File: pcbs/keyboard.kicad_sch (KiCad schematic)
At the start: 214 parts, among them J1 MJ-4PP-9, J2 MJ-4PP-9, SW1 SW_PUSH, SW2 SW_PUSH, SW3 RotaryEncoder_Switch, U1 ProMicro, U3 ProMicro

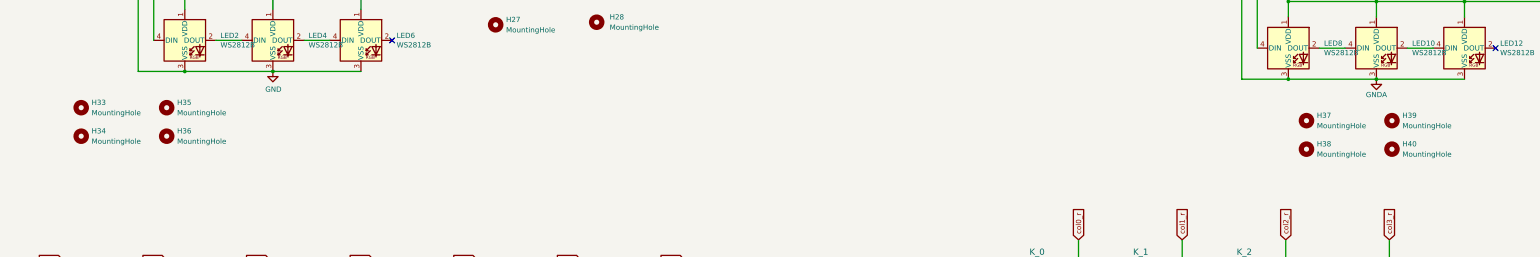
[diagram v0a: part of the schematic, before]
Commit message: Branch for a split jlcpcb order.
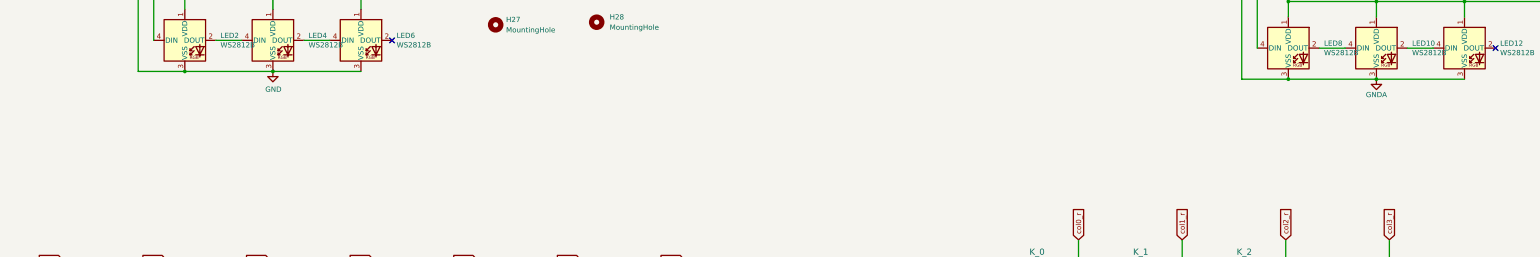
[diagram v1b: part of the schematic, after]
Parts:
- removed H33, H34, H35, H36, H37, H38, H39, H40: MountingHole, Keebio-Parts:breakaway-mousebites_fat-o-tesa, symbol Mechanical:MountingHole
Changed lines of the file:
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@@
     )
   )
-  (symbol (lib_id "Mechanical:MountingHole") (at 380.365 146.05 0) (unit 1)
-    (in_bom yes) (on_board yes) (dnp no) (fields_autoplaced)
-    (property "Reference" "H37" (at 382.905 144.78 0)
-      (effects (font (size 1.27 1.27)) (justify left))
-    )
-    (property "Value" "MountingHole" (at 382.905 147.32 0)
-      (effects (font (size 1.27 1.27)) (justify left))
-    )
-    (property "Footprint" "Keebio-Parts:breakaway-mousebites_fat-o-tesa" (at 380.365 146.05 0)
-      (effects (font (size 1.27 1.27)) hide)
-    )
-    (property "Datasheet" "~" (at 380.365 146.05 0)
-      (effects (font (size 1.27 1.27)) hide)
-    )
-    (instances
-      (project "keyboard"
-        (path "/30eea16d-cbc8-4652-9fea-1af3eb5fea52"
-          (reference "H37") (unit 1)
-        )
-      )
-    )
-  )
   (symbol (lib_id "Mechanical:MountingHole") (at 412.115 60.325 0) (unit 1)
     (in_bom yes) (on_board yes) (dnp no) (fields_autoplaced)
@@
     )
   )
-  (symbol (lib_id "Mechanical:MountingHole") (at 100.965 142.875 0) (unit 1)
-    (in_bom yes) (on_board yes) (dnp no) (fields_autoplaced)
-    (property "Reference" "H35" (at 103.505 141.605 0)
-      (effects (font (size 1.27 1.27)) (justify left))
-    )
-    (property "Value" "MountingHole" (at 103.505 144.145 0)
-      (effects (font (size 1.27 1.27)) (justify left))
-    )
-    (property "Footprint" "Keebio-Parts:breakaway-mousebites_fat-o-tesa" (at 100.965 142.875 0)
-      (effects (font (size 1.27 1.27)) hide)
-    )
-    (property "Datasheet" "~" (at 100.965 142.875 0)
-      (effects (font (size 1.27 1.27)) hide)
-    )
-    (instances
-      (project "keyboard"
-        (path "/30eea16d-cbc8-4652-9fea-1af3eb5fea52"
-          (reference "H35") (unit 1)
-        )
-      )
-    )
-  )
   (symbol (lib_id "Device:D_Small") (at 89.535 323.85 90) (unit 1)
     (in_bom yes) (on_board yes) (dnp no)
@@
     )
   )
-  (symbol (lib_id "Mechanical:MountingHole") (at 401.32 153.035 0) (unit 1)
-    (in_bom yes) (on_board yes) (dnp no) (fields_autoplaced)
-    (property "Reference" "H40" (at 403.86 151.765 0)
-      (effects (font (size 1.27 1.27)) (justify left))
-    )
-    (property "Value" "MountingHole" (at 403.86 154.305 0)
-      (effects (font (size 1.27 1.27)) (justify left))
-    )
-    (property "Footprint" "Keebio-Parts:breakaway-mousebites_fat-o-tesa" (at 401.32 153.035 0)
-      (effects (font (size 1.27 1.27)) hide)
-    )
-    (property "Datasheet" "~" (at 401.32 153.035 0)
-      (effects (font (size 1.27 1.27)) hide)
-    )
-    (instances
-      (project "keyboard"
-        (path "/30eea16d-cbc8-4652-9fea-1af3eb5fea52"
-          (reference "H40") (unit 1)
-        )
-      )
-    )
-  )
   (symbol (lib_id "MX_Alps_Hybrid:MX-NoLED") (at 167.005 265.43 0) (unit 1)
     (in_bom yes) (on_board yes) (dnp no)
@@
     )
   )
-  (symbol (lib_id "Mechanical:MountingHole") (at 380.365 153.035 0) (unit 1)
-    (in_bom yes) (on_board yes) (dnp no) (fields_autoplaced)
-    (property "Reference" "H38" (at 382.905 151.765 0)
-      (effects (font (size 1.27 1.27)) (justify left))
-    )
-    (property "Value" "MountingHole" (at 382.905 154.305 0)
-      (effects (font (size 1.27 1.27)) (justify left))
-    )
-    (property "Footprint" "Keebio-Parts:breakaway-mousebites_fat-o-tesa" (at 380.365 153.035 0)
-      (effects (font (size 1.27 1.27)) hide)
-    )
-    (property "Datasheet" "~" (at 380.365 153.035 0)
-      (effects (font (size 1.27 1.27)) hide)
-    )
-    (instances
-      (project "keyboard"
-        (path "/30eea16d-cbc8-4652-9fea-1af3eb5fea52"
-          (reference "H38") (unit 1)
-        )
-      )
-    )
-  )
   (symbol (lib_id "Device:D_Small") (at 516.255 320.04 90) (unit 1)
     (in_bom yes) (on_board yes) (dnp no)
@@
     )
   )
-  (symbol (lib_id "Mechanical:MountingHole") (at 80.01 142.875 0) (unit 1)
-    (in_bom yes) (on_board yes) (dnp no) (fields_autoplaced)
-    (property "Reference" "H33" (at 82.55 141.605 0)
-      (effects (font (size 1.27 1.27)) (justify left))
-    )
-    (property "Value" "MountingHole" (at 82.55 144.145 0)
-      (effects (font (size 1.27 1.27)) (justify left))
-    )
-    (property "Footprint" "Keebio-Parts:breakaway-mousebites_fat-o-tesa" (at 80.01 142.875 0)
-      (effects (font (size 1.27 1.27)) hide)
-    )
-    (property "Datasheet" "~" (at 80.01 142.875 0)
-      (effects (font (size 1.27 1.27)) hide)
-    )
-    (instances
-      (project "keyboard"
-        (path "/30eea16d-cbc8-4652-9fea-1af3eb5fea52"
-          (reference "H33") (unit 1)
-        )
-      )
-    )
-  )
   (symbol (lib_id "power:GND") (at 107.315 349.25 0) (unit 1)
     (in_bom yes) (on_board yes) (dnp no)
@@
     )
   )
-  (symbol (lib_id "Mechanical:MountingHole") (at 100.965 149.86 0) (unit 1)
-    (in_bom yes) (on_board yes) (dnp no) (fields_autoplaced)
-    (property "Reference" "H36" (at 103.505 148.59 0)
-      (effects (font (size 1.27 1.27)) (justify left))
-    )
-    (property "Value" "MountingHole" (at 103.505 151.13 0)
-      (effects (font (size 1.27 1.27)) (justify left))
-    )
-    (property "Footprint" "Keebio-Parts:breakaway-mousebites_fat-o-tesa" (at 100.965 149.86 0)
-      (effects (font (size 1.27 1.27)) hide)
-    )
-    (property "Datasheet" "~" (at 100.965 149.86 0)
-      (effects (font (size 1.27 1.27)) hide)
-    )
-    (instances
-      (project "keyboard"
-        (path "/30eea16d-cbc8-4652-9fea-1af3eb5fea52"
-          (reference "H36") (unit 1)
-        )
-      )
-    )
-  )
   (symbol (lib_id "PCM_marbastlib-mx:MX_stab") (at 361.315 341.63 0) (unit 1)
     (in_bom yes) (on_board yes) (dnp no) (fields_autoplaced)
@@
     )
   )
-  (symbol (lib_id "Mechanical:MountingHole") (at 80.01 149.86 0) (unit 1)
-    (in_bom yes) (on_board yes) (dnp no) (fields_autoplaced)
-    (property "Reference" "H34" (at 82.55 148.59 0)
-      (effects (font (size 1.27 1.27)) (justify left))
-    )
-    (property "Value" "MountingHole" (at 82.55 151.13 0)
-      (effects (font (size 1.27 1.27)) (justify left))
-    )
-    (property "Footprint" "Keebio-Parts:breakaway-mousebites_fat-o-tesa" (at 80.01 149.86 0)
-      (effects (font (size 1.27 1.27)) hide)
-    )
-    (property "Datasheet" "~" (at 80.01 149.86 0)
-      (effects (font (size 1.27 1.27)) hide)
-    )
-    (instances
-      (project "keyboard"
-        (path "/30eea16d-cbc8-4652-9fea-1af3eb5fea52"
-          (reference "H34") (unit 1)
-        )
-      )
-    )
-  )
   (symbol (lib_id "Mechanical:MountingHole") (at 159.385 81.915 0) (unit 1)
     (in_bom yes) (on_board yes) (dnp no)
@@
         )
       )
-    )
-  )
-  (symbol (lib_id "Mechanical:MountingHole") (at 401.32 146.05 0) (unit 1)
-    (in_bom yes) (on_board yes) (dnp no) (fields_autoplaced)
-    (property "Reference" "H39" (at 403.86 144.78 0)
-      (effects (font (size 1.27 1.27)) (justify left))
-    )
-    (property "Value" "MountingHole" (at 403.86 147.32 0)
-      (effects (font (size 1.27 1.27)) (justify left))
-    )
-    (property "Footprint" "Keebio-Parts:breakaway-mousebites_fat-o-tesa" (at 401.32 146.05 0)
-      (effects (font (size 1.27 1.27)) hide)
-    )
-    (property "Datasheet" "~" (at 401.32 146.05 0)
-      (effects (font (size 1.27 1.27)) hide)
-    )
-    (instances
-      (project "keyboard"
-        (path "/30eea16d-cbc8-4652-9fea-1af3eb5fea52"
-          (reference "H39") (unit 1)
-        )
-      )
